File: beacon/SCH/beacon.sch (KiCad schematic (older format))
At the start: 8 parts, among them U1 74LS14, U2 LM555N

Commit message: transmitter added
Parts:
- added P1: CONNECTOR, symbol CONNECTOR
- added U3: QFM-TX1, symbol QFM-TX1
- renumbered C2 to C1, C1 to C2, U2 to U1, U1 to U2
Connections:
- net DATA: now also U3.4 (DATA)
- net ENABLE: now also U3.3 (ENABLE)
- net GND: now also U3.2 (GND), U3.5 (GND)
- net VCC: now also U3.1 (VCC)
- new net: P1.1 (W), U3.6 (ANT)
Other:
- moved on the sheet: BT1, C1, C2, R1, R2, TH1, U1, U2A, U2B

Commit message: schematic cleanup
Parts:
- renumbered C2 to C1, C1 to C2, U2 to U1, U1 to U2
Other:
- moved on the sheet: C1
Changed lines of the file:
@@
 $EndDescr
 $Comp
-L LM555N U1
+L LM555N U2
 U 1 1 540DF191
 P 1850 3700
-F 0 "U1" H 1850 3800 70  0000 C CNN
+F 0 "U2" H 1850 3800 70  0000 C CNN
 F 1 "LM555N" H 1850 3600 70  0000 C CNN
 F 2 "" H 1850 3700 60  0000 C CNN
@@
 $EndComp
 $Comp
-L C C1
+L C C2
 U 1 1 540DF1E1
 P 2600 4150
-F 0 "C1" H 2600 4250 40  0000 L CNN
+F 0 "C2" H 2600 4250 40  0000 L CNN
 F 1 "C" H 2606 4065 40  0000 L CNN
 F 2 "" H 2638 4000 30  0000 C CNN
@@
 $EndComp
 $Comp
-L VCC #PWR7
+L VCC #PWR2
 U 1 1 540DF661
 P 10100 3300
-F 0 "#PWR7" H 10100 3400 30  0001 C CNN
+F 0 "#PWR2" H 10100 3400 30  0001 C CNN
 F 1 "VCC" H 10100 3400 30  0000 C CNN
 F 2 "" H 10100 3300 60  0000 C CNN
@@
 $EndComp
 $Comp
-L GND #PWR8
+L GND #PWR5
 U 1 1 540DF675
 P 10100 4000
-F 0 "#PWR8" H 10100 4000 30  0001 C CNN
+F 0 "#PWR5" H 10100 4000 30  0001 C CNN
 F 1 "GND" H 10100 3930 30  0001 C CNN
 F 2 "" H 10100 4000 60  0000 C CNN
@@
 $EndComp
 $Comp
-L GND #PWR2
+L GND #PWR7
 U 1 1 540DFB7D
 P 2600 4450
-F 0 "#PWR2" H 2600 4450 30  0001 C CNN
+F 0 "#PWR7" H 2600 4450 30  0001 C CNN
 F 1 "GND" H 2600 4380 30  0001 C CNN
 F 2 "" H 2600 4450 60  0000 C CNN
@@
 	3300 3700 3250 3700
 $Comp
-L VCC #PWR1
+L VCC #PWR4
 U 1 1 540DFBD8
 P 1100 4000
-F 0 "#PWR1" H 1100 4100 30  0001 C CNN
+F 0 "#PWR4" H 1100 4100 30  0001 C CNN
 F 1 "VCC" H 1100 4100 30  0000 C CNN
 F 2 "" H 1100 4000 60  0000 C CNN
@@
 	1150 4000 1100 4000
 $Comp
-L 74LS14 U2
+L 74LS14 U1
 U 1 1 540DFD5D
 P 3750 3500
-F 0 "U2" H 3900 3600 40  0000 C CNN
+F 0 "U1" H 3900 3600 40  0000 C CNN
 F 1 "74LS14" H 3950 3400 40  0000 C CNN
 F 2 "" H 3750 3500 60  0000 C CNN
@@
 	1150 3250 1150 3500
 Connection ~ 2600 3900
-Wire Wire Line
-	2750 3700 2750 3800
-Wire Wire Line
-	2750 3800 3250 3800
-Connection ~ 2750 3700
-$Comp
-L 74LS14 U2
+$Comp
+L 74LS14 U1
 U 2 1 540E02E8
 P 5300 3650
-F 0 "U2" H 5450 3750 40  0000 C CNN
+F 0 "U1" H 5450 3750 40  0000 C CNN
 F 1 "74LS14" H 5500 3550 40  0000 C CNN
 F 2 "" H 5300 3650 60  0000 C CNN
@@
 $EndComp
 Wire Wire Line
-	5750 3650 5750 3250
-Wire Wire Line
-	5750 3250 5500 3250
-Wire Wire Line
-	5000 3250 4850 3250
-Wire Wire Line
-	4850 3250 4850 3700
-$Comp
-L C C2
+	5500 3250 5800 3250
+Wire Wire Line
+	4800 3250 5000 3250
+$Comp
+L C C1
 U 1 1 540E052B
-P 4850 3900
-F 0 "C2" H 4850 4000 40  0000 L CNN
-F 1 "C" H 4856 3815 40  0000 L CNN
-F 2 "" H 4888 3750 30  0000 C CNN
-F 3 "" H 4850 3900 60  0000 C CNN
-	1    4850 3900
+P 4800 3900
+F 0 "C1" H 4800 4000 40  0000 L CNN
+F 1 "C" H 4806 3815 40  0000 L CNN
+F 2 "" H 4838 3750 30  0000 C CNN
+F 3 "" H 4800 3900 60  0000 C CNN
+	1    4800 3900
 	-1   0    0    1
 $EndComp
-Connection ~ 4850 3650
-$Comp
-L GND #PWR4
+$Comp
+L GND #PWR6
 U 1 1 540E062C
-P 4850 4150
-F 0 "#PWR4" H 4850 4150 30  0001 C CNN
-F 1 "GND" H 4850 4080 30  0001 C CNN
-F 2 "" H 4850 4150 60  0000 C CNN
-F 3 "" H 4850 4150 60  0000 C CNN
-	1    4850 4150
-	1    0    0    -1
-$EndComp
-Wire Wire Line
-	4850 4100 4850 4150
-Wire Wire Line
-	5750 3650 5800 3650
-Text GLabel 5800 3650 2    60   Input ~ 0
+P 4800 4150
+F 0 "#PWR6" H 4800 4150 30  0001 C CNN
+F 1 "GND" H 4800 4080 30  0001 C CNN
+F 2 "" H 4800 4150 60  0000 C CNN
+F 3 "" H 4800 4150 60  0000 C CNN
+	1    4800 4150
+	1    0    0    -1
+$EndComp
+Wire Wire Line
+	5750 3650 5850 3650
+Text GLabel 5850 3650 2    60   Input ~ 0
 DATA
 $Comp
@@
 $EndComp
 $Comp
-L GND #PWR6
+L GND #PWR8
 U 1 1 540F475B
-P 8150 4500
-F 0 "#PWR6" H 8150 4500 30  0001 C CNN
-F 1 "GND" H 8150 4430 30  0001 C CNN
-F 2 "" H 8150 4500 60  0000 C CNN
-F 3 "" H 8150 4500 60  0000 C CNN
-	1    8150 4500
-	1    0    0    -1
-$EndComp
-$Comp
-L VCC #PWR5
+P 8150 4550
+F 0 "#PWR8" H 8150 4550 30  0001 C CNN
+F 1 "GND" H 8150 4480 30  0001 C CNN
+F 2 "" H 8150 4550 60  0000 C CNN
+F 3 "" H 8150 4550 60  0000 C CNN
+	1    8150 4550
+	1    0    0    -1
+$EndComp
+$Comp
+L VCC #PWR1
 U 1 1 540F4770
 P 8100 3300
-F 0 "#PWR5" H 8100 3400 30  0001 C CNN
+F 0 "#PWR1" H 8100 3400 30  0001 C CNN
 F 1 "VCC" H 8100 3400 30  0000 C CNN
 F 2 "" H 8100 3300 60  0000 C CNN
@@
 Wire Wire Line
 	7400 3850 7350 3850
-Wire Wire Line
-	8050 4450 8150 4450
-Wire Wire Line
-	8150 4450 8150 4500
-Connection ~ 8150 4450
 Wire Wire Line
 	8100 3350 8100 3300
@@
 Wire Wire Line
 	8850 3900 8800 3900
+Wire Wire Line
+	8150 4450 8150 4550
+Wire Wire Line
+	8050 4450 8050 4500
+Wire Wire Line
+	8050 4500 8150 4500
+Connection ~ 8150 4500
+Wire Wire Line
+	4800 3250 4800 3700
+Wire Wire Line
+	4850 3650 4800 3650
+Connection ~ 4800 3650
+Wire Wire Line
+	5800 3250 5800 3650
+Connection ~ 5800 3650
+Wire Wire Line
+	4800 4100 4800 4150
+Wire Wire Line
+	2700 3700 2700 3800
+Wire Wire Line
+	2700 3800 3250 3800
+Connection ~ 2700 3700
 $EndSCHEMATC

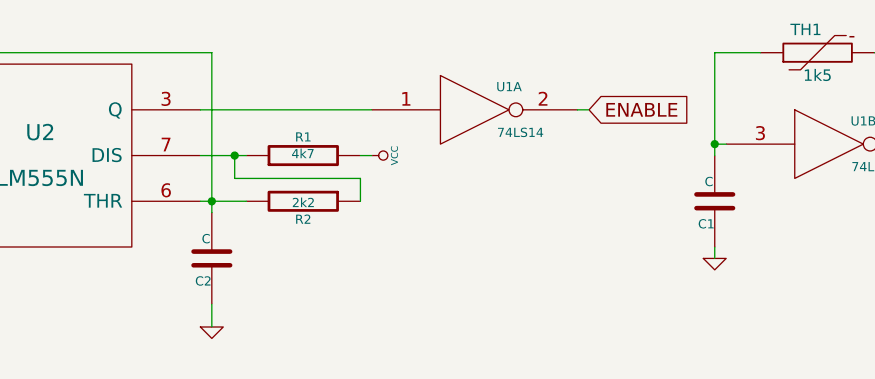
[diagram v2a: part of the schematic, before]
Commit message: capacitor value added
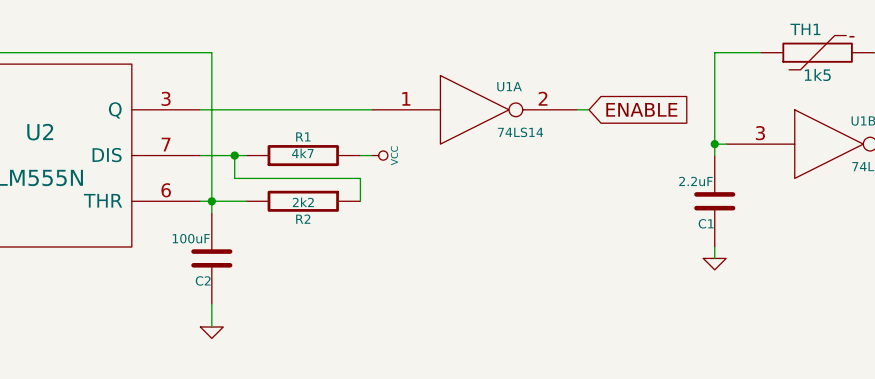
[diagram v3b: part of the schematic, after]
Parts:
- C1: value C -> 2.2uF
- C2: value C -> 100uF
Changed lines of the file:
@@
 P 2600 4150
 F 0 "C2" H 2600 4250 40  0000 L CNN
-F 1 "C" H 2606 4065 40  0000 L CNN
+F 1 "100uF" H 2606 4065 40  0000 L CNN
 F 2 "" H 2638 4000 30  0000 C CNN
 F 3 "" H 2600 4150 60  0000 C CNN
@@
 P 4800 3900
 F 0 "C1" H 4800 4000 40  0000 L CNN
-F 1 "C" H 4806 3815 40  0000 L CNN
+F 1 "2.2uF" H 4806 3815 40  0000 L CNN
 F 2 "" H 4838 3750 30  0000 C CNN
 F 3 "" H 4800 3900 60  0000 C CNN

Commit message: last improvments and pcbs
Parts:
- added C3, C4: 100nF, Capacitors_SMD:C_0805, symbol C
- added unit 3 of U1
- added unit 4 of U1
- added unit 5 of U1
- added unit 6 of U1
- BT1: footprint (none) -> Coin Cell Holder:Coin_Cell_Holder_CH25-2032LF
- C1, C2: footprint (none) -> Capacitors_SMD:C_0805
- P1: footprint (none) -> Pin_Headers:Pin_Header_Straight_1x01
- R1, R2: footprint (none) -> Resistors_SMD:R_0805_HandSoldering
- TH1: footprint (none) -> Capacitors_ThroughHole:Capacitor7x3-5RM5_RevB
- U1: footprint (none) -> SMD_Packages:SOIC-14_W
- U2: footprint (none) -> SMD_Packages:SOIC-8-W
- U3: footprint (none) -> QFM-TX1:QFM-TX1
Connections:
- net GND: now also C3.2, C4.2, U1.11, U1.13, U1.5, U1.7 (GND), U1.7 (GND), U1.7 (GND), U1.7 (GND), U1.9
- net VCC: now also C3.1, C4.1, U1.14 (VCC), U1.14 (VCC), U1.14 (VCC), U1.14 (VCC)
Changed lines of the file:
@@
 F 0 "U2" H 1850 3800 70  0000 C CNN
 F 1 "LM555N" H 1850 3600 70  0000 C CNN
-F 2 "" H 1850 3700 60  0000 C CNN
+F 2 "SMD_Packages:SOIC-8-W" H 1850 3700 60  0001 C CNN
 F 3 "" H 1850 3700 60  0000 C CNN
 	1    1850 3700
@@
 F 0 "C2" H 2600 4250 40  0000 L CNN
 F 1 "100uF" H 2606 4065 40  0000 L CNN
-F 2 "" H 2638 4000 30  0000 C CNN
+F 2 "Capacitors_SMD:C_0805" H 2638 4000 30  0001 C CNN
 F 3 "" H 2600 4150 60  0000 C CNN
 	1    2600 4150
@@
 F 0 "BT1" H 10100 3850 50  0000 C CNN
 F 1 "BATTERY" H 10100 3460 50  0000 C CNN
-F 2 "" H 10100 3650 60  0000 C CNN
+F 2 "Coin Cell Holder:Coin_Cell_Holder_CH25-2032LF" H 10100 3650 60  0001 C CNN
 F 3 "" H 10100 3650 60  0000 C CNN
 	1    10100 3650
@@
 F 0 "R1" V 3080 3700 40  0000 C CNN
 F 1 "4k7" V 3007 3701 40  0000 C CNN
-F 2 "" V 2930 3700 30  0000 C CNN
+F 2 "Resistors_SMD:R_0805_HandSoldering" V 2930 3700 30  0001 C CNN
 F 3 "" H 3000 3700 30  0000 C CNN
 	1    3000 3700
@@
 $EndComp
 $Comp
-L VCC #PWR2
+L VCC #PWR01
 U 1 1 540DF661
 P 10100 3300
-F 0 "#PWR2" H 10100 3400 30  0001 C CNN
+F 0 "#PWR01" H 10100 3400 30  0001 C CNN
 F 1 "VCC" H 10100 3400 30  0000 C CNN
 F 2 "" H 10100 3300 60  0000 C CNN
@@
 $EndComp
 $Comp
-L GND #PWR5
+L GND #PWR02
 U 1 1 540DF675
 P 10100 4000
-F 0 "#PWR5" H 10100 4000 30  0001 C CNN
+F 0 "#PWR02" H 10100 4000 30  0001 C CNN
 F 1 "GND" H 10100 3930 30  0001 C CNN
 F 2 "" H 10100 4000 60  0000 C CNN
@@
 F 0 "R2" V 3080 3900 40  0000 C CNN
 F 1 "2k2" V 3007 3901 40  0000 C CNN
-F 2 "" V 2930 3900 30  0000 C CNN
+F 2 "Resistors_SMD:R_0805_HandSoldering" V 2930 3900 30  0001 C CNN
 F 3 "" H 3000 3900 30  0000 C CNN
 	1    3000 3900
@@
 $EndComp
 $Comp
-L VCC #PWR3
+L VCC #PWR03
 U 1 1 540DFB6D
 P 3300 3700
-F 0 "#PWR3" H 3300 3800 30  0001 C CNN
+F 0 "#PWR03" H 3300 3800 30  0001 C CNN
 F 1 "VCC" H 3300 3800 30  0000 C CNN
 F 2 "" H 3300 3700 60  0000 C CNN
@@
 $EndComp
 $Comp
-L GND #PWR7
+L GND #PWR04
 U 1 1 540DFB7D
 P 2600 4450
-F 0 "#PWR7" H 2600 4450 30  0001 C CNN
+F 0 "#PWR04" H 2600 4450 30  0001 C CNN
 F 1 "GND" H 2600 4380 30  0001 C CNN
 F 2 "" H 2600 4450 60  0000 C CNN
@@
 	3300 3700 3250 3700
 $Comp
-L VCC #PWR4
+L VCC #PWR05
 U 1 1 540DFBD8
 P 1100 4000
-F 0 "#PWR4" H 1100 4100 30  0001 C CNN
+F 0 "#PWR05" H 1100 4100 30  0001 C CNN
 F 1 "VCC" H 1100 4100 30  0000 C CNN
 F 2 "" H 1100 4000 60  0000 C CNN
@@
 F 0 "U1" H 3900 3600 40  0000 C CNN
 F 1 "74LS14" H 3950 3400 40  0000 C CNN
-F 2 "" H 3750 3500 60  0000 C CNN
+F 2 "SMD_Packages:SOIC-14_W" H 3750 3500 60  0001 C CNN
 F 3 "" H 3750 3500 60  0000 C CNN
 	1    3750 3500
@@
 F 0 "U1" H 5450 3750 40  0000 C CNN
 F 1 "74LS14" H 5500 3550 40  0000 C CNN
-F 2 "" H 5300 3650 60  0000 C CNN
+F 2 "SMD_Packages:SOIC-14_W" H 5300 3650 60  0001 C CNN
 F 3 "" H 5300 3650 60  0000 C CNN
 	2    5300 3650
@@
 F 0 "TH1" V 5350 3300 50  0000 C CNN
 F 1 "1k5" V 5150 3250 50  0000 C CNN
-F 2 "" H 5250 3250 60  0000 C CNN
+F 2 "Capacitors_ThroughHole:Capacitor7x3-5RM5_RevB" H 5250 3250 60  0001 C CNN
 F 3 "" H 5250 3250 60  0000 C CNN
 	1    5250 3250
@@
 F 0 "C1" H 4800 4000 40  0000 L CNN
 F 1 "2.2uF" H 4806 3815 40  0000 L CNN
-F 2 "" H 4838 3750 30  0000 C CNN
+F 2 "Capacitors_SMD:C_0805" H 4838 3750 30  0001 C CNN
 F 3 "" H 4800 3900 60  0000 C CNN
 	1    4800 3900
@@
 $EndComp
 $Comp
-L GND #PWR6
+L GND #PWR06
 U 1 1 540E062C
 P 4800 4150
-F 0 "#PWR6" H 4800 4150 30  0001 C CNN
+F 0 "#PWR06" H 4800 4150 30  0001 C CNN
 F 1 "GND" H 4800 4080 30  0001 C CNN
 F 2 "" H 4800 4150 60  0000 C CNN
@@
 F 0 "U3" H 8450 3550 60  0000 C CNN
 F 1 "QFM-TX1" H 8350 4250 60  0000 C CNN
-F 2 "" H 7250 3300 60  0000 C CNN
+F 2 "QFM-TX1:QFM-TX1" H 7250 3300 60  0001 C CNN
 F 3 "" H 7250 3300 60  0000 C CNN
 	1    8100 3900
@@
 $EndComp
 $Comp
-L GND #PWR8
+L GND #PWR07
 U 1 1 540F475B
 P 8150 4550
-F 0 "#PWR8" H 8150 4550 30  0001 C CNN
+F 0 "#PWR07" H 8150 4550 30  0001 C CNN
 F 1 "GND" H 8150 4480 30  0001 C CNN
 F 2 "" H 8150 4550 60  0000 C CNN
@@
 $EndComp
 $Comp
-L VCC #PWR1
+L VCC #PWR08
 U 1 1 540F4770
 P 8100 3300
-F 0 "#PWR1" H 8100 3400 30  0001 C CNN
+F 0 "#PWR08" H 8100 3400 30  0001 C CNN
 F 1 "VCC" H 8100 3400 30  0000 C CNN
 F 2 "" H 8100 3300 60  0000 C CNN
@@
 F 0 "P1" H 9200 4000 70  0000 C CNN
 F 1 "CONNECTOR" H 9200 3800 70  0000 C CNN
-F 2 "" H 8850 3900 60  0000 C CNN
+F 2 "Pin_Headers:Pin_Header_Straight_1x01" H 8850 3900 60  0001 C CNN
 F 3 "" H 8850 3900 60  0000 C CNN
 	1    8850 3900
@@
 	2700 3800 3250 3800
 Connection ~ 2700 3700
+$Comp
+L C C3
+U 1 1 541CBBDE
+P 9350 5000
+F 0 "C3" H 9350 5100 40  0000 L CNN
+F 1 "100nF" H 9356 4915 40  0000 L CNN
+F 2 "Capacitors_SMD:C_0805" H 9388 4850 30  0001 C CNN
+F 3 "" H 9350 5000 60  0000 C CNN
+	1    9350 5000
+	1    0    0    -1
+$EndComp
+$Comp
+L C C4
+U 1 1 541CBE70
+P 9650 5000
+F 0 "C4" H 9650 5100 40  0000 L CNN
+F 1 "100nF" H 9656 4915 40  0000 L CNN
+F 2 "Capacitors_SMD:C_0805" H 9688 4850 30  0001 C CNN
+F 3 "" H 9650 5000 60  0000 C CNN
+	1    9650 5000
+	1    0    0    -1
+$EndComp
+Wire Wire Line
+	9350 4800 9350 4750
+Wire Wire Line
+	9350 4750 9650 4750
+Wire Wire Line
+	9650 4750 9650 4800
+Wire Wire Line
+	9650 5200 9650 5250
+Wire Wire Line
+	9650 5250 9350 5250
+Wire Wire Line
+	9350 5250 9350 5200
+$Comp
+L GND #PWR09
+U 1 1 541CBF74
+P 9500 5300
+F 0 "#PWR09" H 9500 5300 30  0001 C CNN
+F 1 "GND" H 9500 5230 30  0001 C CNN
+F 2 "" H 9500 5300 60  0000 C CNN
+F 3 "" H 9500 5300 60  0000 C CNN
+	1    9500 5300
+	1    0    0    -1
+$EndComp
+$Comp
+L VCC #PWR010
+U 1 1 541CBFB3
+P 9500 4700
+F 0 "#PWR010" H 9500 4800 30  0001 C CNN
+F 1 "VCC" H 9500 4800 30  0000 C CNN
+F 2 "" H 9500 4700 60  0000 C CNN
+F 3 "" H 9500 4700 60  0000 C CNN
+	1    9500 4700
+	1    0    0    -1
+$EndComp
+Wire Wire Line
+	9500 5300 9500 5250
+Connection ~ 9500 5250
+Wire Wire Line
+	9500 4700 9500 4750
+Connection ~ 9500 4750
+$Comp
+L 74LS14 U1
+U 3 1 541CC21B
+P 4500 5000
+F 0 "U1" H 4650 5100 40  0000 C CNN
+F 1 "74LS14" H 4700 4900 40  0000 C CNN
+F 2 "" H 4500 5000 60  0000 C CNN
+F 3 "" H 4500 5000 60  0000 C CNN
+	3    4500 5000
+	1    0    0    -1
+$EndComp
+$Comp
+L 74LS14 U1
+U 4 1 541CC49E
+P 4500 5400
+F 0 "U1" H 4650 5500 40  0000 C CNN
+F 1 "74LS14" H 4700 5300 40  0000 C CNN
+F 2 "" H 4500 5400 60  0000 C CNN
+F 3 "" H 4500 5400 60  0000 C CNN
+	4    4500 5400
+	1    0    0    -1
+$EndComp
+$Comp
+L 74LS14 U1
+U 5 1 541CC4E6
+P 4500 5800
+F 0 "U1" H 4650 5900 40  0000 C CNN
+F 1 "74LS14" H 4700 5700 40  0000 C CNN
+F 2 "" H 4500 5800 60  0000 C CNN
+F 3 "" H 4500 5800 60  0000 C CNN
+	5    4500 5800
+	1    0    0    -1
+$EndComp
+$Comp
+L 74LS14 U1
+U 6 1 541CC51F
+P 4500 6200
+F 0 "U1" H 4650 6300 40  0000 C CNN
+F 1 "74LS14" H 4700 6100 40  0000 C CNN
+F 2 "" H 4500 6200 60  0000 C CNN
+F 3 "" H 4500 6200 60  0000 C CNN
+	6    4500 6200
+	1    0    0    -1
+$EndComp
+$Comp
+L GND #PWR011
+U 1 1 541CC58E
+P 4000 6300
+F 0 "#PWR011" H 4000 6300 30  0001 C CNN
+F 1 "GND" H 4000 6230 30  0001 C CNN
+F 2 "" H 4000 6300 60  0000 C CNN
+F 3 "" H 4000 6300 60  0000 C CNN
+	1    4000 6300
+	1    0    0    -1
+$EndComp
+Wire Wire Line
+	4000 5000 4000 6300
+Wire Wire Line
+	4000 6200 4050 6200
+Wire Wire Line
+	4050 5800 4000 5800
+Connection ~ 4000 6200
+Wire Wire Line
+	4050 5400 4000 5400
+Connection ~ 4000 5800
+Wire Wire Line
+	4050 5000 4000 5000
+Connection ~ 4000 5400
 $EndSCHEMATC
